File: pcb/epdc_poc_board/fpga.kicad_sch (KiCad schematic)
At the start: 33 parts, among them J201 Conn_02x05_Odd_Even, U201 ECP5U_45_CABGA256, U202 W25Q128JVP, Y201 24MHz

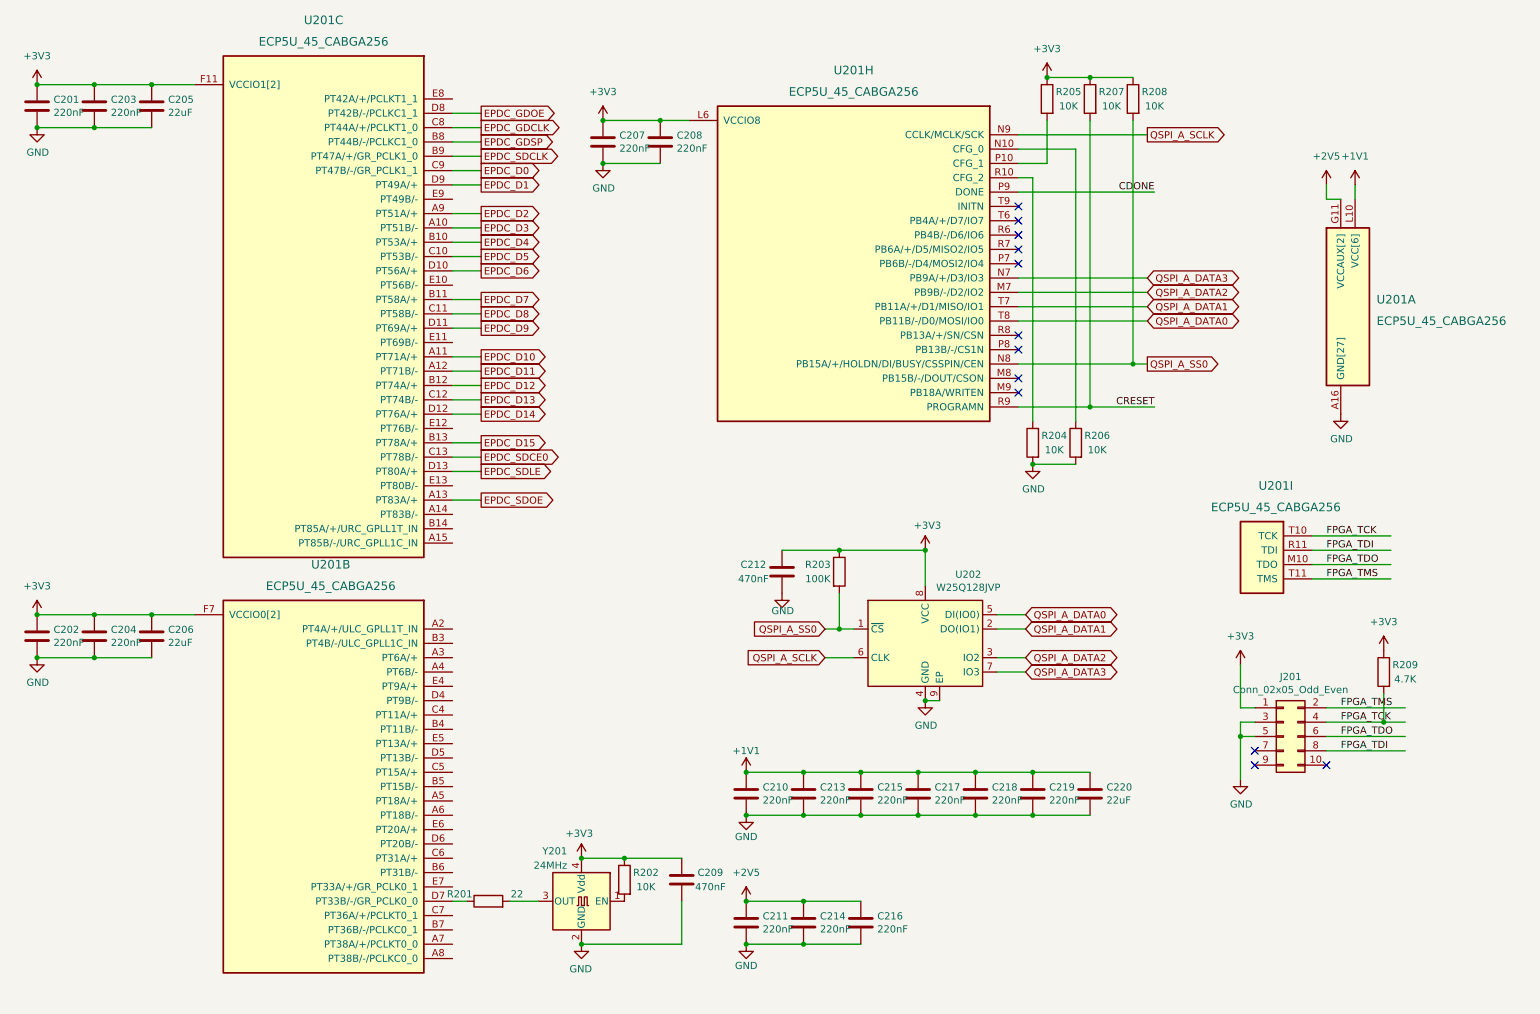
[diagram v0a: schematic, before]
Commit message: - wip epdc poc board, going to remove vga input
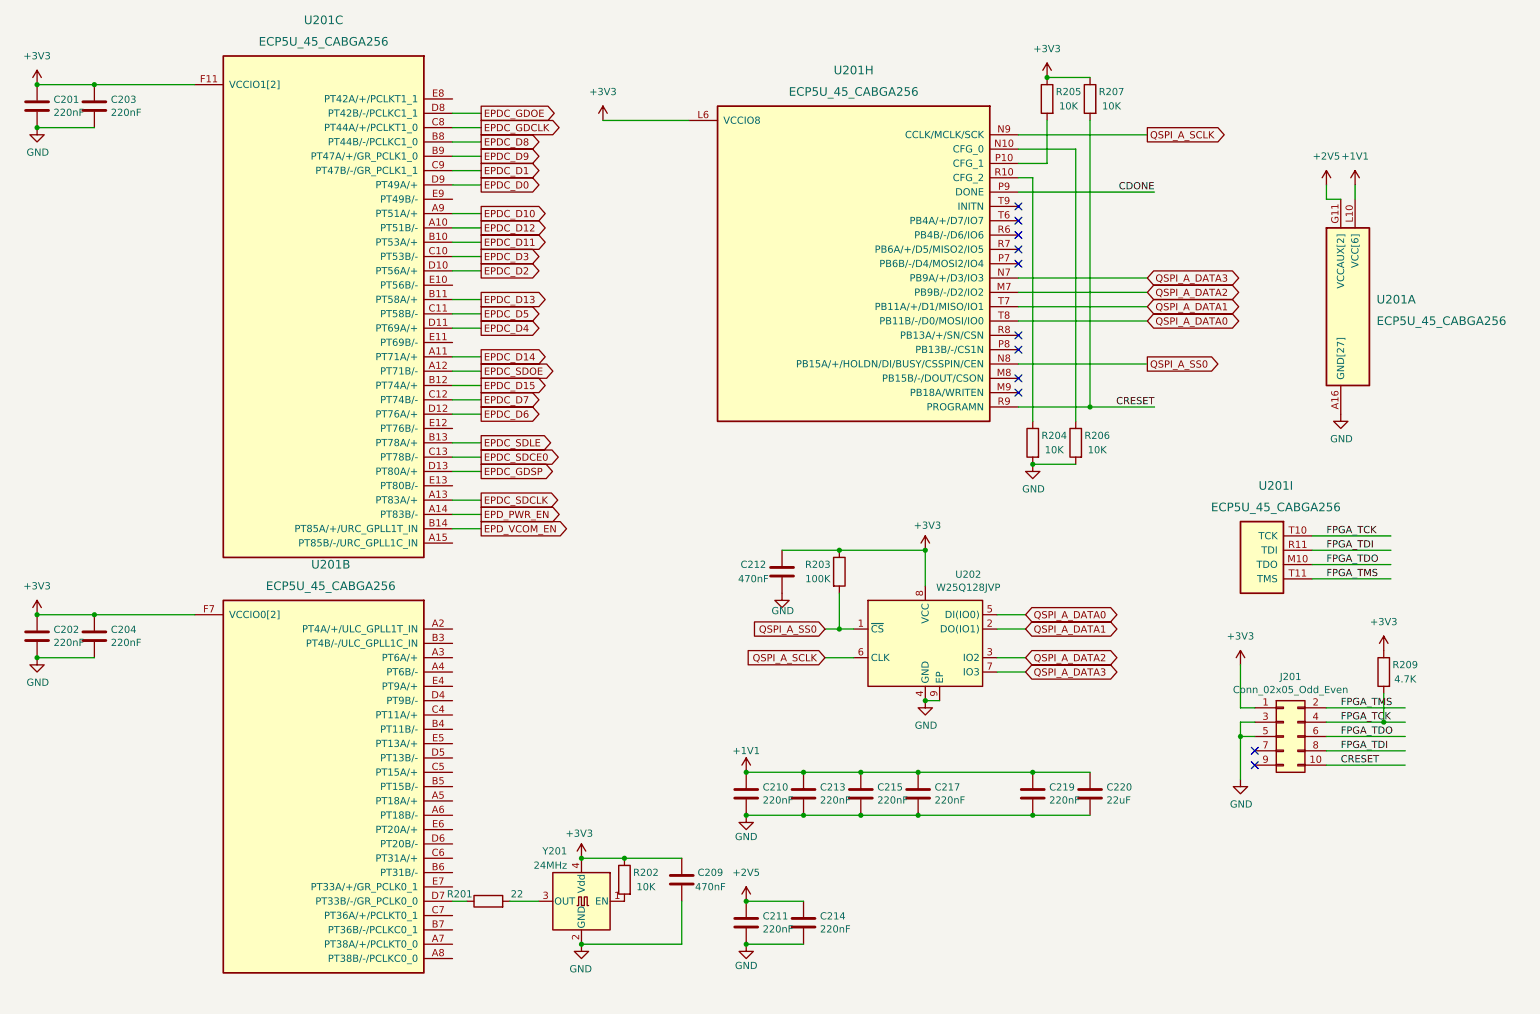
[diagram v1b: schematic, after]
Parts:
- removed C205, C206: 22uF, Capacitor_SMD:C_0603_1608Metric, symbol Device:C
- removed C207, C208, C216, C218: 220nF, Capacitor_SMD:C_0402_1005Metric, symbol Device:C
- removed R208: 10K, Capacitor_SMD:C_0402_1005Metric, symbol Device:R
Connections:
- net CRESET: now also J201.10 (Pin_10)
- net EPDC_D0: now also U201.D9 (PT49A/+); no longer U201.C9 (PT47B/-/GR_PCLK1_1)
- net EPDC_D1: now also U201.C9 (PT47B/-/GR_PCLK1_1); no longer U201.D9 (PT49A/+)
- net EPDC_D10: now also U201.A9 (PT51A/+); no longer U201.A11 (PT71A/+)
- net EPDC_D11: now also U201.B10 (PT53A/+); no longer U201.A12 (PT71B/-)
- net EPDC_D12: now also U201.A10 (PT51B/-); no longer U201.B12 (PT74A/+)
- net EPDC_D13: now also U201.B11 (PT58A/+); no longer U201.C12 (PT74B/-)
- net EPDC_D14: now also U201.A11 (PT71A/+); no longer U201.D12 (PT76A/+)
- net EPDC_D15: now also U201.B12 (PT74A/+); no longer U201.B13 (PT78A/+)
- net EPDC_D2: now also U201.D10 (PT56A/+); no longer U201.A9 (PT51A/+)
- net EPDC_D3: now also U201.C10 (PT53B/-); no longer U201.A10 (PT51B/-)
- net EPDC_D4: now also U201.D11 (PT69A/+); no longer U201.B10 (PT53A/+)
- net EPDC_D5: now also U201.C11 (PT58B/-); no longer U201.C10 (PT53B/-)
- net EPDC_D6: now also U201.D12 (PT76A/+); no longer U201.D10 (PT56A/+)
- net EPDC_D7: now also U201.C12 (PT74B/-); no longer U201.B11 (PT58A/+)
- net EPDC_D8: now also U201.B8 (PT44B/-/PCLKC1_0); no longer U201.C11 (PT58B/-)
- net EPDC_D9: now also U201.B9 (PT47A/+/GR_PCLK1_0); no longer U201.D11 (PT69A/+)
- net EPDC_GDSP: now also U201.D13 (PT80A/+); no longer U201.B8 (PT44B/-/PCLKC1_0)
- net EPDC_SDCLK: now also U201.A13 (PT83A/+); no longer U201.B9 (PT47A/+/GR_PCLK1_0)
- net EPDC_SDLE: now also U201.B13 (PT78A/+); no longer U201.D13 (PT80A/+)
- net EPDC_SDOE: now also U201.A12 (PT71B/-); no longer U201.A13 (PT83A/+)
- net EPD_PWR_EN: now reaches U201.A14 (PT83B/-)
- net EPD_VCOM_EN: now reaches U201.B14 (PT85A/+/URC_GPLL1T_IN)
- no-connect marks 12 -> 11

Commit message: pcb: switch to s6 for epdc board
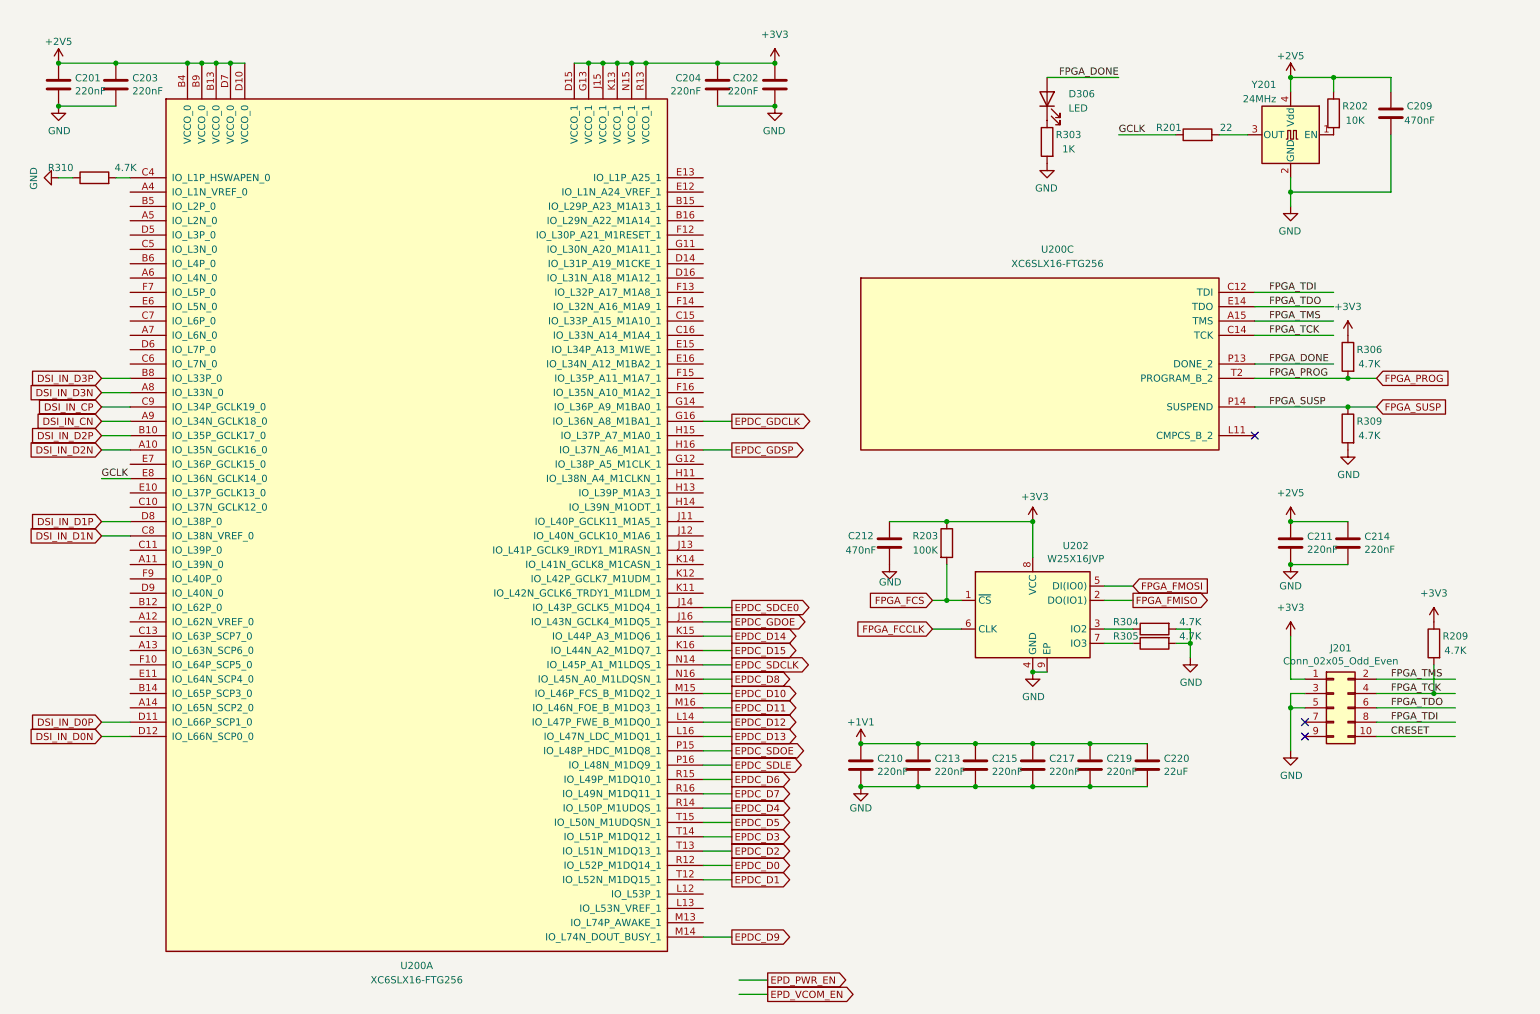
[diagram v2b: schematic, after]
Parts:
- removed R204, R205, R206, R207: 10K, Capacitor_SMD:C_0402_1005Metric, symbol Device:R
- removed U201: ECP5U_45_CABGA256, Package_BGA:BGA-256_14.0x14.0mm_Layout16x16_P0.8mm_Ball0.45mm_Pad0.32mm_NSMD, symbol symbols:ECP5U_45_CABGA256
- added D306: LED, LED_SMD:LED_0603_1608Metric, symbol Device:LED
- added R303: 1K, Resistor_SMD:R_0402_1005Metric, symbol Device:R
- added R304, R305, R306, R309, R310: 4.7K, Resistor_SMD:R_0402_1005Metric, symbol Device:R
- added U200: XC6SLX16-FTG256, Package_BGA:BGA-256_14.0x14.0mm_Layout16x16_P0.8mm_Ball0.45mm_Pad0.32mm_NSMD, symbol FPGA_Xilinx_Spartan6:XC6SLX16-FTG256
- U202: value W25Q128JVP -> W25X16JVP
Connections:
- net +2V5: now also C201.1, C203.1, C209.2, R202.1, Y201.4 (Vdd), U200.B13 (VCCO_0), U200.B4 (VCCO_0), U200.B9 (VCCO_0), U200.D10 (VCCO_0), U200.D7 (VCCO_0)
- net +3V3: now also R306.1, U200.D15 (VCCO_1), U200.G13 (VCCO_1), U200.J15 (VCCO_1), U200.K13 (VCCO_1), U200.N15 (VCCO_1), U200.R13 (VCCO_1); no longer C201.1, C203.1, C209.2, R202.1, Y201.4 (Vdd)
- net EPDC_D0: now also U200.R12 (IO_L52P_M1DQ14_1)
- net EPDC_D1: now also U200.T12 (IO_L52N_M1DQ15_1)
- net EPDC_D10: now also U200.M15 (IO_L46P_FCS_B_M1DQ2_1)
- net EPDC_D11: now also U200.M16 (IO_L46N_FOE_B_M1DQ3_1)
- net EPDC_D12: now also U200.L14 (IO_L47P_FWE_B_M1DQ0_1)
- net EPDC_D13: now also U200.L16 (IO_L47N_LDC_M1DQ1_1)
- net EPDC_D14: now also U200.K15 (IO_L44P_A3_M1DQ6_1)
- net EPDC_D15: now also U200.K16 (IO_L44N_A2_M1DQ7_1)
- net EPDC_D2: now also U200.T13 (IO_L51N_M1DQ13_1)
- net EPDC_D3: now also U200.T14 (IO_L51P_M1DQ12_1)
- net EPDC_D4: now also U200.R14 (IO_L50P_M1UDQS_1)
- net EPDC_D5: now also U200.T15 (IO_L50N_M1UDQSN_1)
- net EPDC_D6: now also U200.R15 (IO_L49P_M1DQ10_1)
- net EPDC_D7: now also U200.R16 (IO_L49N_M1DQ11_1)
- net EPDC_D8: now also U200.N16 (IO_L45N_A0_M1LDQSN_1)
- net EPDC_D9: now also U200.M14 (IO_L74N_DOUT_BUSY_1)
- net EPDC_GDCLK: now also U200.G16 (IO_L36N_A8_M1BA1_1)
- net EPDC_GDOE: now also U200.J16 (IO_L43N_GCLK4_M1DQ5_1)
- net EPDC_GDSP: now also U200.H16 (IO_L37N_A6_M1A1_1)
- net EPDC_SDCE0: now also U200.J14 (IO_L43P_GCLK5_M1DQ4_1)
- net EPDC_SDCLK: now also U200.N14 (IO_L45P_A1_M1LDQS_1)
- net EPDC_SDLE: now also U200.P16 (IO_L48N_M1DQ9_1)
- net EPDC_SDOE: now also U200.P15 (IO_L48P_HDC_M1DQ8_1)
- net FPGA_TCK: now also U200.C14 (TCK)
- net FPGA_TDI: now also U200.C12 (TDI)
- net FPGA_TDO: now also U200.E14 (TDO)
- net FPGA_TMS: now also U200.A15 (TMS)
- net GND: now also R303.2, R304.2, R305.2, R309.2, R310.1
- net GCLK: now reaches R201.1
- net GCLK: now also U200.E8 (IO_L36N_GCLK14_0)
- net QSPI_A_DATA0 renamed FPGA_FMOSI
- net QSPI_A_DATA1 renamed FPGA_FMISO
- net QSPI_A_DATA2: no longer names the net of U202.3 (IO2)
- net QSPI_A_DATA2: now also R304.1
- net QSPI_A_DATA3: no longer names the net of U202.7 (IO3)
- net QSPI_A_DATA3: now also R305.1
- net QSPI_A_SCLK renamed FPGA_FCCLK
- net QSPI_A_SS0 renamed FPGA_FCS
- new net: D306.1 (K), R303.1
- new net: R310.2, U200.C4 (IO_L1P_HSWAPEN_0)
- new net DSI_IN_CN: U200.A9 (IO_L34N_GCLK18_0)
- new net DSI_IN_CP: U200.C9 (IO_L34P_GCLK19_0)
- new net DSI_IN_D0N: U200.D12 (IO_L66N_SCP0_0)
- new net DSI_IN_D0P: U200.D11 (IO_L66P_SCP1_0)
- new net DSI_IN_D1N: U200.C8 (IO_L38N_VREF_0)
- new net DSI_IN_D1P: U200.D8 (IO_L38P_0)
- new net DSI_IN_D2N: U200.A10 (IO_L35N_GCLK16_0)
- new net DSI_IN_D2P: U200.B10 (IO_L35P_GCLK17_0)
- new net DSI_IN_D3N: U200.A8 (IO_L33N_0)
- new net DSI_IN_D3P: U200.B8 (IO_L33P_0)
- new net FPGA_DONE: D306.2 (A), U200.P13 (DONE_2)
- new net FPGA_PROG: R306.2, U200.T2 (PROGRAM_B_2)
- new net FPGA_SUSP: R309.1, U200.P14 (SUSPEND)
- no-connect marks 11 -> 3
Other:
- moved on the sheet: C201, C202, C203, C204, C210, C211, C212, C213, C214, C215, C217, C219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

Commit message: pcb: mb r0.1, caster r0.1 freeze
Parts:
- C201, C202, C203, C204, C210, C211, C213, C214, C215, C217, C219: LCSC (none) -> C880414; Ref.Price (none) -> 0.0036
- C209, C212: value 470nF -> 220nF; LCSC (none) -> C880414; Ref.Price (none) -> 0.0036
- C220: LCSC (none) -> C94018; Ref.Price (none) -> 0.0301
- D306: LCSC (none) -> C90692; Ref.Price (none) -> 0.0176
- J201: LCSC (none) -> -; Ref.Price (none) -> 0
- R201: value 22 -> 22R; footprint Capacitor_SMD:C_0402_1005Metric -> Resistor_SMD:R_0402_1005Metric; LCSC (none) -> C93929; Ref.Price (none) -> 0.002
- R202: value 10K -> 4.7K; footprint Capacitor_SMD:C_0402_1005Metric -> Resistor_SMD:R_0402_1005Metric; LCSC (none) -> C105870; Ref.Price (none) -> 0.0006
- R203: value 100K -> 49.9K/1%; footprint Capacitor_SMD:C_0402_1005Metric -> Resistor_SMD:R_0402_1005Metric; LCSC (none) -> C137969; Ref.Price (none) -> 0.001
- R209, R304, R305, R306, R309, R310: LCSC (none) -> C105870; Ref.Price (none) -> 0.0006
- R303: LCSC (none) -> C105637; Ref.Price (none) -> 0.0006
- U200: LCSC (none) -> C39313; Ref.Price (none) -> 7.4837
- U202: LCSC (none) -> C571260; Ref.Price (none) -> 0.9559
- Y201: LCSC (none) -> C252339; Ref.Price (none) -> 0.5014
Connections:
- net DSI_IN_CN is gone; now on net DSI_IN_D1N: U200.A9 (IO_L34N_GCLK18_0)
- net DSI_IN_CP is gone; now on net DSI_IN_D1P: U200.C9 (IO_L34P_GCLK19_0)
- net DSI_IN_D0N: now also U200.A8 (IO_L33N_0); no longer U200.D12 (IO_L66N_SCP0_0)
- net DSI_IN_D0P: now also U200.B8 (IO_L33P_0); no longer U200.D11 (IO_L66P_SCP1_0)
- net DSI_IN_D1N: no longer U200.C8 (IO_L38N_VREF_0)
- net DSI_IN_D1P: no longer U200.D8 (IO_L38P_0)
- net DSI_IN_D2N: now also U200.C8 (IO_L38N_VREF_0); no longer U200.A10 (IO_L35N_GCLK16_0)
- net DSI_IN_D2P: now also U200.D8 (IO_L38P_0); no longer U200.B10 (IO_L35P_GCLK17_0)
- net DSI_IN_D3N: now also U200.D12 (IO_L66N_SCP0_0); no longer U200.A8 (IO_L33N_0)
- net DSI_IN_D3P: now also U200.D11 (IO_L66P_SCP1_0); no longer U200.B8 (IO_L33P_0)
- new net DSI_IN_CKN: U200.A10 (IO_L35N_GCLK16_0)
- new net DSI_IN_CKP: U200.B10 (IO_L35P_GCLK17_0)
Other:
- company: (none) -> Copyright 2021 Modos / Engineer: Wenting Zhang
- title: (none) -> Caster EPDC
